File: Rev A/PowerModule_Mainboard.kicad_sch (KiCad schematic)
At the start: 0 parts

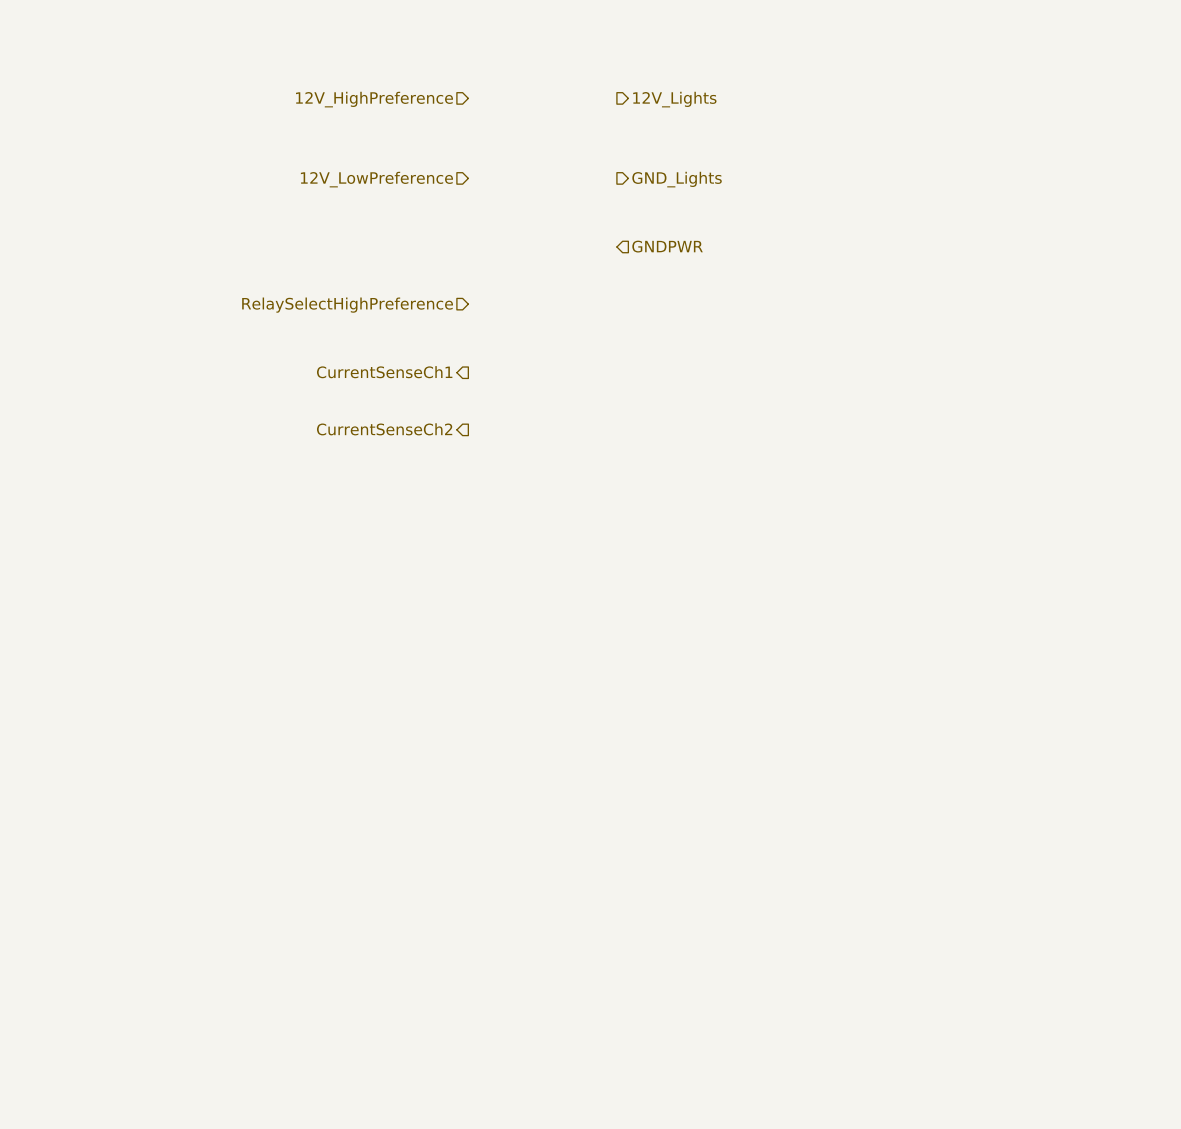
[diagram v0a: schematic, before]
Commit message: Added power Module, started layout
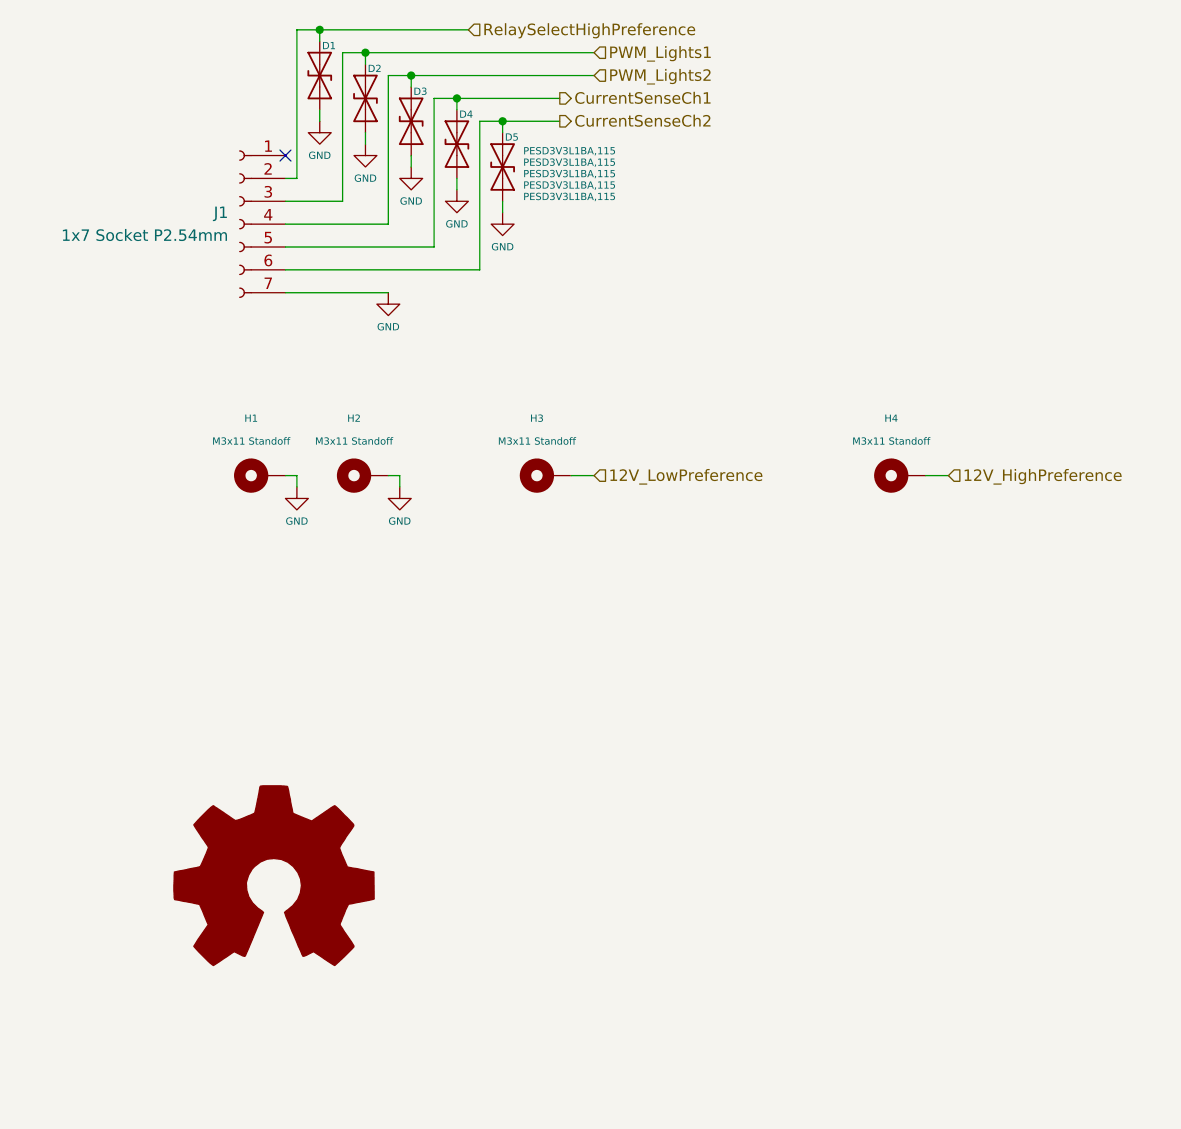
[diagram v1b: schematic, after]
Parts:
- added D1, D2, D3, D4, D5: PESD3V3L1BA,115, Diode_SMD:D_SOD-323F, symbol Diode:SMAJ5.0CA
- added H1, H2, H3, H4: M3x11 Standoff, Mounting_Wuerth:Mounting_Wuerth_WA-SMSI-M3_H11mm_9774110360, symbol Mechanical:MountingHole_Pad
- added J1: 1x7 Socket P2.54mm, Connector_PinHeader_2.54mm:PinHeader_1x07_P2.54mm_Vertical, symbol Connector:Conn_01x07_Socket
- added SYM1: Logo_Open_Hardware_Large, Symbol:OSHW-Logo_38.1x40mm_SilkScreen, symbol Graphic:Logo_Open_Hardware_Large
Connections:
- net 12V_HighPreference: now also H4.1
- net 12V_LowPreference: now also H3.1
- net CurrentSenseCh1: now also D4.2 (A2), J1.5 (Pin_5)
- net CurrentSenseCh2: now also D5.2 (A2), J1.6 (Pin_6)
- net RelaySelectHighPreference: now also D1.2 (A2), J1.2 (Pin_2)
- new net GND: D1.1 (A1), D2.1 (A1), D3.1 (A1), D4.1 (A1), D5.1 (A1), H1.1, H2.1, J1.7 (Pin_7)
- new net PWM_Lights1: D2.2 (A2), J1.3 (Pin_3)
- new net PWM_Lights2: D3.2 (A2), J1.4 (Pin_4)
- no-connect marks 0 -> 1

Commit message: yes
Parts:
- removed D1, D2, D3, D4, D5: PESD3V3L1BA,115, Diode_SMD:D_SOD-323F, symbol Diode:SMAJ5.0CA
- removed J1: 1x7 Socket P2.54mm, Connector_PinHeader_2.54mm:PinHeader_1x07_P2.54mm_Vertical, symbol Connector:Conn_01x07_Socket
- removed SYM1: Logo_Open_Hardware_Large, Symbol:OSHW-Logo_38.1x40mm_SilkScreen, symbol Graphic:Logo_Open_Hardware_Large
- added J1: 2x7 P2.54mm, Connector_PinSocket_2.54mm:PinSocket_2x07_P2.54mm_Vertical, symbol Connector_Generic:Conn_02x07_Odd_Even
- added SYM2: SYM_Hot_Small, Modules_SurgicalLighting:PowerModule, symbol Graphic:SYM_Hot_Small
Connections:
- net CurrentSenseCh1: now also J1.10 (Pin_10), J1.9 (Pin_9)
- net CurrentSenseCh2: now also J1.11 (Pin_11), J1.12 (Pin_12)
- net GND: now also J1.13 (Pin_13), J1.14 (Pin_14)
- net PWM_Lights1: now also J1.5 (Pin_5), J1.6 (Pin_6)
- net PWM_Lights2: now also J1.7 (Pin_7), J1.8 (Pin_8)
- net RelaySelectHighPreference: now also J1.3 (Pin_3), J1.4 (Pin_4)
- new net: J1.1 (Pin_1), J1.2 (Pin_2)
